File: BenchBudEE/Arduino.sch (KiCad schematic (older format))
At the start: 0 parts

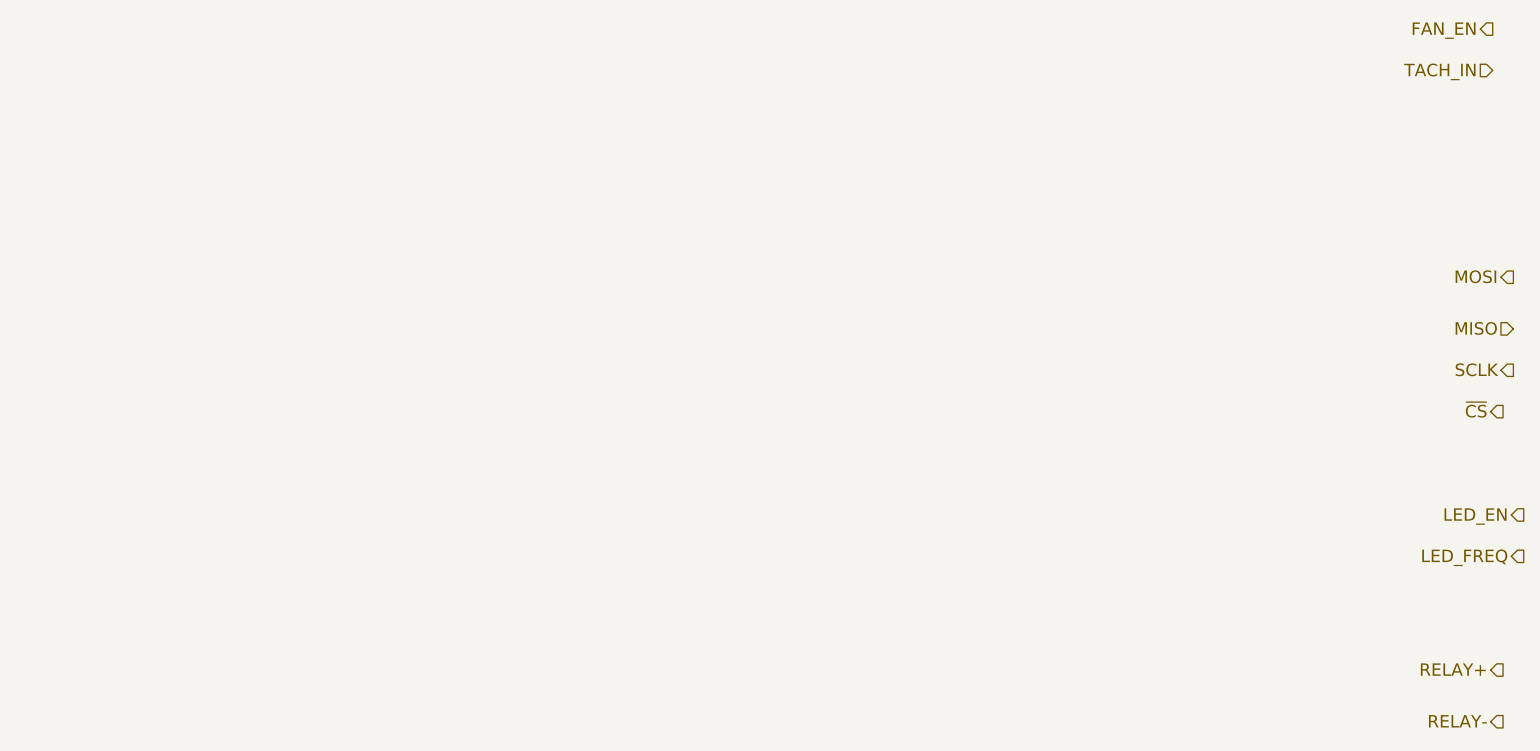
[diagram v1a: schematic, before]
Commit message: arduino schematic and interconnection
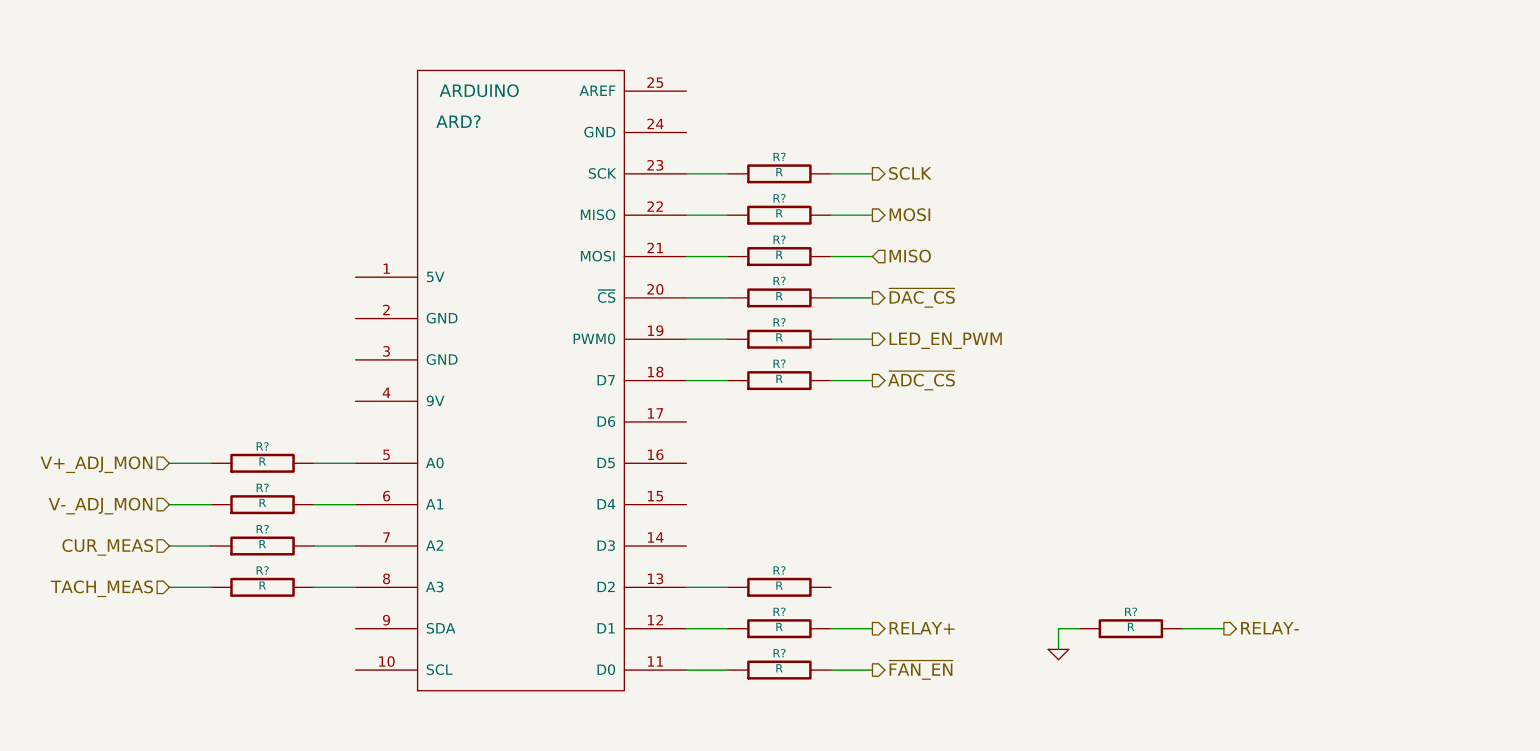
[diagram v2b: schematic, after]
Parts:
- added ARD?: ARDUINO, symbol ARDUINO
- added R? (x14): R, ~, symbol R
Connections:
- net MISO: now also R?.2
- net MOSI: now also R?.2
- net RELAY+: now also R?.2
- net RELAY-: now also R?.2
- net SCLK: now also R?.2
- new net: ARD?.11 (D0), R?.1
- new net: ARD?.12 (D1), R?.1
- new net: ARD?.13 (D2), R?.1
- new net: ARD?.18 (D7), R?.1
- new net: ARD?.19 (PWM0), R?.1
- new net: ARD?.20 (~CS), R?.1
- new net: ARD?.21 (MOSI), R?.1
- new net: ARD?.22 (MISO), R?.1
- new net: ARD?.23 (SCK), R?.1
- new net: ARD?.5 (A0), R?.2
- new net: ARD?.6 (A1), R?.2
- new net: ARD?.7 (A2), R?.2
- new net: ARD?.8 (A3), R?.2
- new net CUR_MEAS: R?.1
- new net GND: R?.1
- new net LED_EN_PWM: R?.2
- new net TACH_MEAS: R?.1
- new net V+_ADJ_MON: R?.1
- new net V-_ADJ_MON: R?.1
- new net ~ADC_CS: R?.2
- new net ~DAC_CS: R?.2
- new net ~FAN_EN: R?.2

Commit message: fan/current supply refactor
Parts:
- removed R?: R, ~, symbol R
- added R? (x2): R, ~, symbol R
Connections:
- net at R?.1: now also ARD?.20 (~CS); no longer ARD?.11 (D0)
- net at ARD?.17 (D6): now also R?.1
- net at ARD?.4 (9V): now also R?.2
- net ~FAN_EN renamed FAN_PWM
- new net: ARD?.11 (D0), R?.1
- new net +12P: R?.1
- new net FAN_MODE: R?.2
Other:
- moved on the sheet: R?
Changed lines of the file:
@@
 Text HLabel 6600 2600 2    60   Output ~ 0
 SCLK
-Text HLabel 6600 3200 2    60   Output ~ 0
+Text HLabel 6600 3800 2    60   Output ~ 0
 ~DAC_CS
 Text HLabel 3200 4600 0    60   Input ~ 0
 TACH_MEAS
-Text HLabel 6600 5000 2    60   Output ~ 0
-~FAN_EN
+Text HLabel 6600 3200 2    60   Output ~ 0
+FAN_PWM
 $Comp
 L R R?
 U 1 1 5301DD5B
-P 6150 5000
-F 0 "R?" V 6230 5000 40  0000 C CNN
-F 1 "R" V 6157 5001 40  0000 C CNN
-F 2 "~" V 6080 5000 30  0000 C CNN
-F 3 "~" H 6150 5000 30  0000 C CNN
-	1    6150 5000
-	0    -1   -1   0
-$EndComp
-Wire Wire Line
-	6600 5000 6400 5000
-Wire Wire Line
-	5900 5000 5700 5000
+P 6150 3200
+F 0 "R?" V 6230 3200 40  0000 C CNN
+F 1 "R" V 6157 3201 40  0000 C CNN
+F 2 "~" V 6080 3200 30  0000 C CNN
+F 3 "~" H 6150 3200 30  0000 C CNN
+	1    6150 3200
+	0    -1   -1   0
+$EndComp
+Wire Wire Line
+	6600 3200 6400 3200
+Wire Wire Line
+	5900 3200 5700 3200
 $Comp
 L ARDUINO ARD?
@@
 	0    -1   -1   0
 $EndComp
-$Comp
-L R R?
-U 1 1 5301E229
-P 6150 4600
-F 0 "R?" V 6230 4600 40  0000 C CNN
-F 1 "R" V 6157 4601 40  0000 C CNN
-F 2 "~" V 6080 4600 30  0000 C CNN
-F 3 "~" H 6150 4600 30  0000 C CNN
-	1    6150 4600
-	0    -1   -1   0
-$EndComp
-Wire Wire Line
-	5900 4600 5700 4600
 Wire Wire Line
 	5700 4800 5900 4800
@@
 L R R?
 U 1 1 530222AC
-P 6150 3200
-F 0 "R?" V 6230 3200 40  0000 C CNN
-F 1 "R" V 6157 3201 40  0000 C CNN
-F 2 "~" V 6080 3200 30  0000 C CNN
-F 3 "~" H 6150 3200 30  0000 C CNN
-	1    6150 3200
+P 6150 3800
+F 0 "R?" V 6230 3800 40  0000 C CNN
+F 1 "R" V 6157 3801 40  0000 C CNN
+F 2 "~" V 6080 3800 30  0000 C CNN
+F 3 "~" H 6150 3800 30  0000 C CNN
+	1    6150 3800
 	0    -1   -1   0
 $EndComp
@@
 	5900 3000 5700 3000
 Wire Wire Line
-	5700 3200 5900 3200
-Wire Wire Line
-	6400 3200 6600 3200
+	5700 3800 5900 3800
+Wire Wire Line
+	6400 3800 6600 3800
 Wire Wire Line
 	6600 3000 6400 3000
@@
 Wire Wire Line
 	5900 3600 5700 3600
+$Comp
+L R R?
+U 1 1 5302BB63
+P 6150 5000
+F 0 "R?" V 6230 5000 40  0000 C CNN
+F 1 "R" V 6157 5001 40  0000 C CNN
+F 2 "~" V 6080 5000 30  0000 C CNN
+F 3 "~" H 6150 5000 30  0000 C CNN
+	1    6150 5000
+	0    -1   -1   0
+$EndComp
+Wire Wire Line
+	5900 5000 5700 5000
+Wire Wire Line
+	6400 5000 6600 5000
+Text HLabel 6600 5000 2    60   Output ~ 0
+FAN_MODE
+$Comp
+L R R?
+U 1 1 5302C500
+P 3650 3700
+F 0 "R?" V 3730 3700 40  0000 C CNN
+F 1 "R" V 3657 3701 40  0000 C CNN
+F 2 "~" V 3580 3700 30  0000 C CNN
+F 3 "~" H 3650 3700 30  0000 C CNN
+	1    3650 3700
+	0    -1   -1   0
+$EndComp
+Wire Wire Line
+	3900 3700 4100 3700
+Wire Wire Line
+	3400 3700 3200 3700
+$Comp
+L +12P #PWR?
+U 1 1 5302C556
+P 3200 3650
+F 0 "#PWR?" H 3200 3620 30  0001 C CNN
+F 1 "+12P" H 3200 3750 30  0000 C CNN
+F 2 "" H 3200 3650 60  0000 C CNN
+F 3 "" H 3200 3650 60  0000 C CNN
+	1    3200 3650
+	1    0    0    -1
+$EndComp
+Wire Wire Line
+	3200 3700 3200 3650
 $EndSCHEMATC
